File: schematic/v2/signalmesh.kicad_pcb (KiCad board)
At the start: 4 copper layers, 387 x 151 mm, 155 parts, among them J1 FPGA I/O, J10 INA219_CONFIG, J11 INA219_CONFIG, J12 AAM_DBG, J13 UUM_DBG, J14 ACM_DBG, J15 INA219_CONFIG, J16 DSM_DBG, J17 LCD_display, J18 LCD_display, J19 AudioJack3, J2 FPGA I/O, J3 LCD_display, J4 TDM_DBG, J5 INA219_CONFIG, J6 INA219_CONFIG, J7 INA219_CONFIG, J8 FPGA I/O, J9 FPGA I/O, U1 NUCLEO-H753ZI, U10 INA219AxD, U11 INA219AxD, U12 INA219AxD, U13 INA219AxD, U14 W25Q128JVS, U15 AP2112K-3.3, U16 74HC4050D, U17 NUCLEO-H753ZI, U18 HDSP-7503, U19 HDSP-7503, U2 HDSP-7503, U20 INA219AxD, U21 74HC4050D, U22 AP2112K-3.3, U23 W25Q128JVS, U24 74HC4050D, U25 AP2112K-3.3, U26 W25Q128JVS, U27 MCP2551-I-P, U28 74LVC1G3157, U29 MCP2551-I-P, U3 NUCLEO-F303RE, U30 MCP2551-I-P, U31 MCP2551-I-P, U4 YAAJ_BluePill_Part_Like, U5 24LC256-I_SN, U6 BME280, U7 INA219AxD, U8 24LC256-I_SN, U9 NUCLEO-F446RE

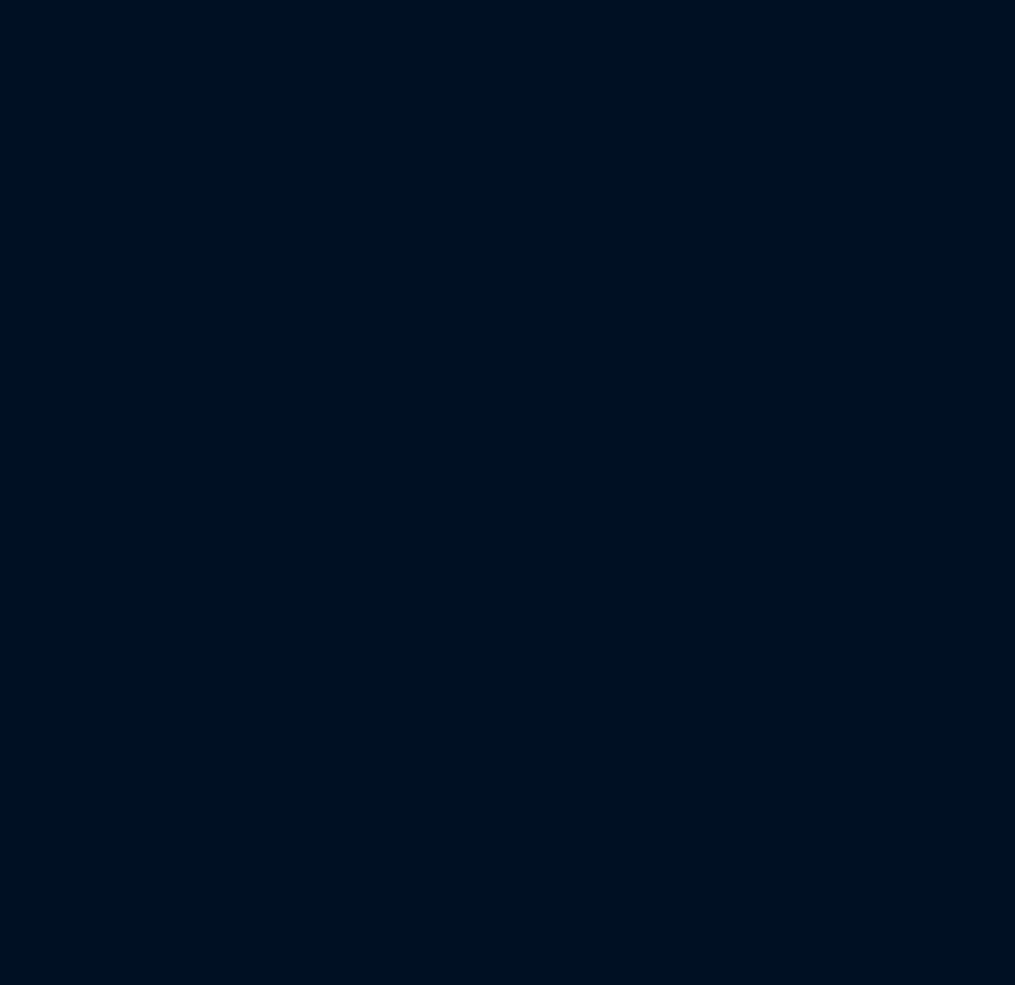
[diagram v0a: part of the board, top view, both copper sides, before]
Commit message: removing the courtyard from the filler plots. theyre not actually components just an outline with throughholes
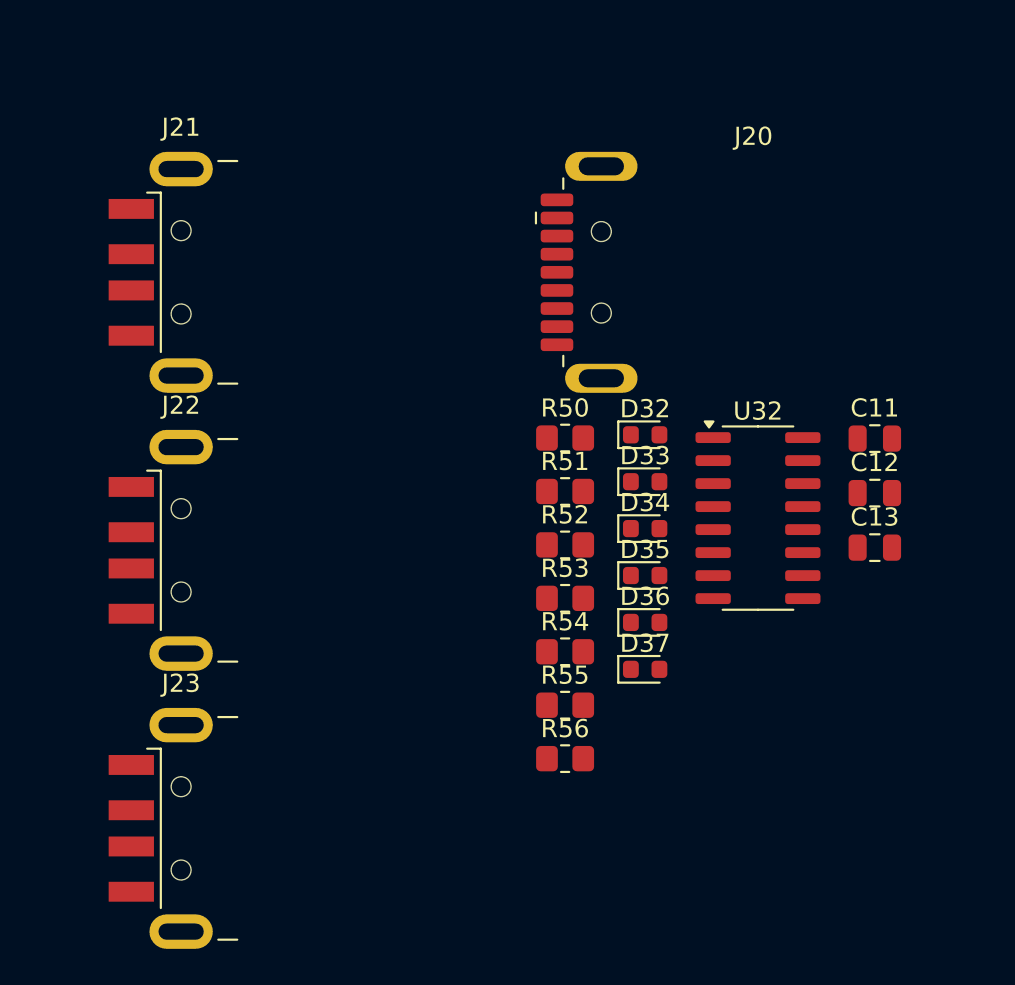
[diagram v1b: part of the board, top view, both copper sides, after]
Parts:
- added C11: 22pf, Capacitor_SMD:C_0805_2012Metric, F.Cu at (338.4, 232.9)
- added C12: 22pf, Capacitor_SMD:C_0805_2012Metric, F.Cu at (338.4, 235.9)
- added C13: 22pf, Capacitor_SMD:C_0805_2012Metric, F.Cu at (338.4, 238.9)
- added D32: LED_PWR, LED_SMD:LED_0603_1608Metric, F.Cu at (325.7, 232.7)
- added D33: LED_PWR, LED_SMD:LED_0603_1608Metric, F.Cu at (325.7, 235.3)
- added D34: LED_PWR, LED_SMD:LED_0603_1608Metric, F.Cu at (325.7, 237.9)
- added D35: TXD, LED_SMD:LED_0603_1608Metric, F.Cu at (325.7, 240.5)
- added D36: RXD, LED_SMD:LED_0603_1608Metric, F.Cu at (325.7, 243.1)
- added D37: LED_PWR, LED_SMD:LED_0603_1608Metric, F.Cu at (325.7, 245.7)
- added J20: USB3_A, Connector_USB:USB3_A_Plug_Wuerth_692112030100_Horizontal, F.Cu at (331.7, 223.8)
- added J21: USB_A, Connector_USB:USB_A_CNCTech_1001-011-01101_Horizontal, F.Cu at (307.0, 223.8)
- added J22: USB_A, Connector_USB:USB_A_CNCTech_1001-011-01101_Horizontal, F.Cu at (307.0, 239.1)
- added J23: USB_A, Connector_USB:USB_A_CNCTech_1001-011-01101_Horizontal, F.Cu at (307.0, 254.4)
- added R50: 300, Resistor_SMD:R_0805_2012Metric_Pad1.20x1.40mm_HandSolder, F.Cu at (321.3, 232.9)
- added R51: 300, Resistor_SMD:R_0805_2012Metric_Pad1.20x1.40mm_HandSolder, F.Cu at (321.3, 235.8)
- added R52: 300, Resistor_SMD:R_0805_2012Metric_Pad1.20x1.40mm_HandSolder, F.Cu at (321.3, 238.8)
- added R53: 300, Resistor_SMD:R_0805_2012Metric_Pad1.20x1.40mm_HandSolder, F.Cu at (321.3, 241.8)
- added R54: 300, Resistor_SMD:R_0805_2012Metric_Pad1.20x1.40mm_HandSolder, F.Cu at (321.3, 244.7)
- added R55: 1k5, Resistor_SMD:R_0805_2012Metric_Pad1.20x1.40mm_HandSolder, F.Cu at (321.3, 247.7)
- added R56: 300, Resistor_SMD:R_0805_2012Metric_Pad1.20x1.40mm_HandSolder, F.Cu at (321.3, 250.6)
- added U32: CH340G, Package_SO:SOIC-16_3.9x9.9mm_P1.27mm, F.Cu at (331.9, 237.3)
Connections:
- U1 pad CN12_12: unconnected-(U1B-PA12-PadCN12_12) -> AAM_USB_D-
- U1 pad CN12_14: unconnected-(U1B-PA11-PadCN12_14) -> AAM_USB_D+

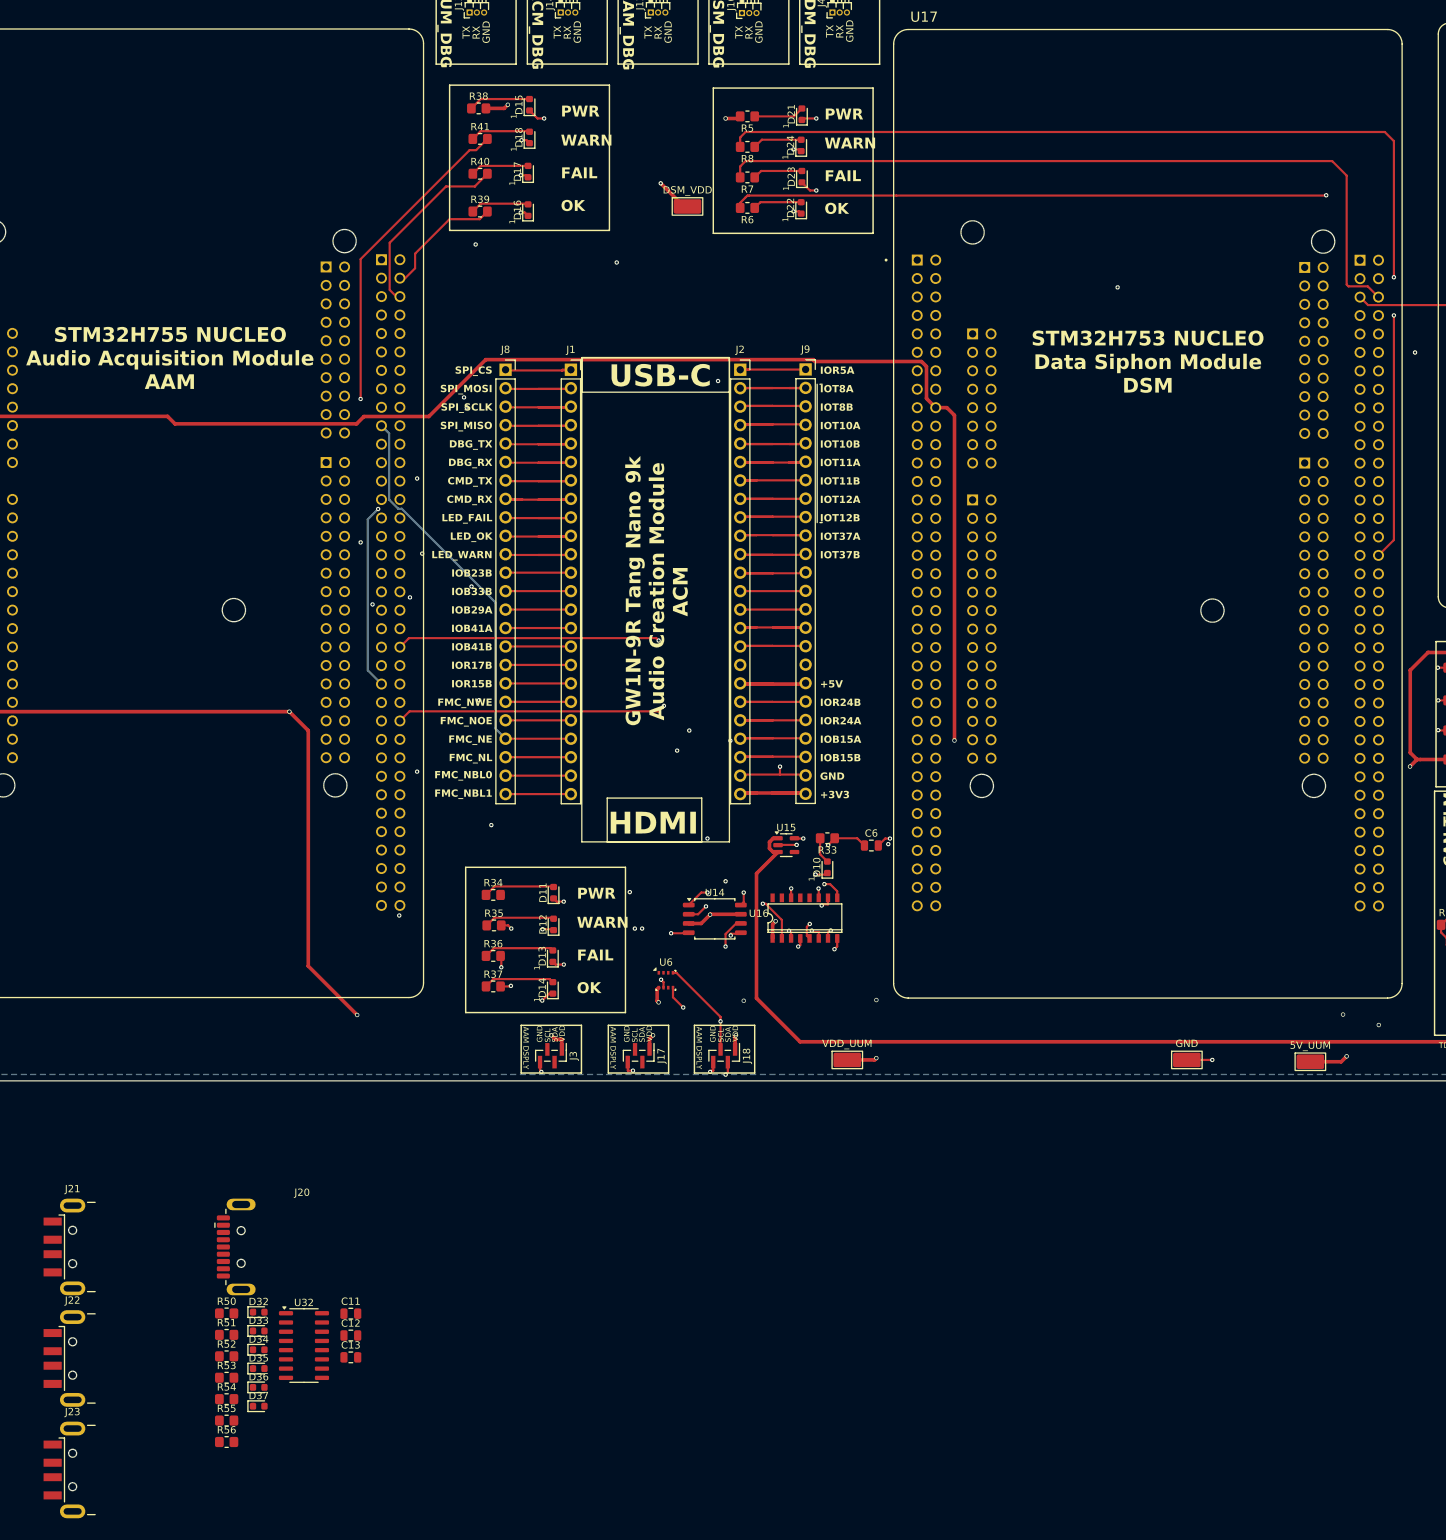
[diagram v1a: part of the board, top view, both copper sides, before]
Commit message: moving to multiple sheets for the schematic
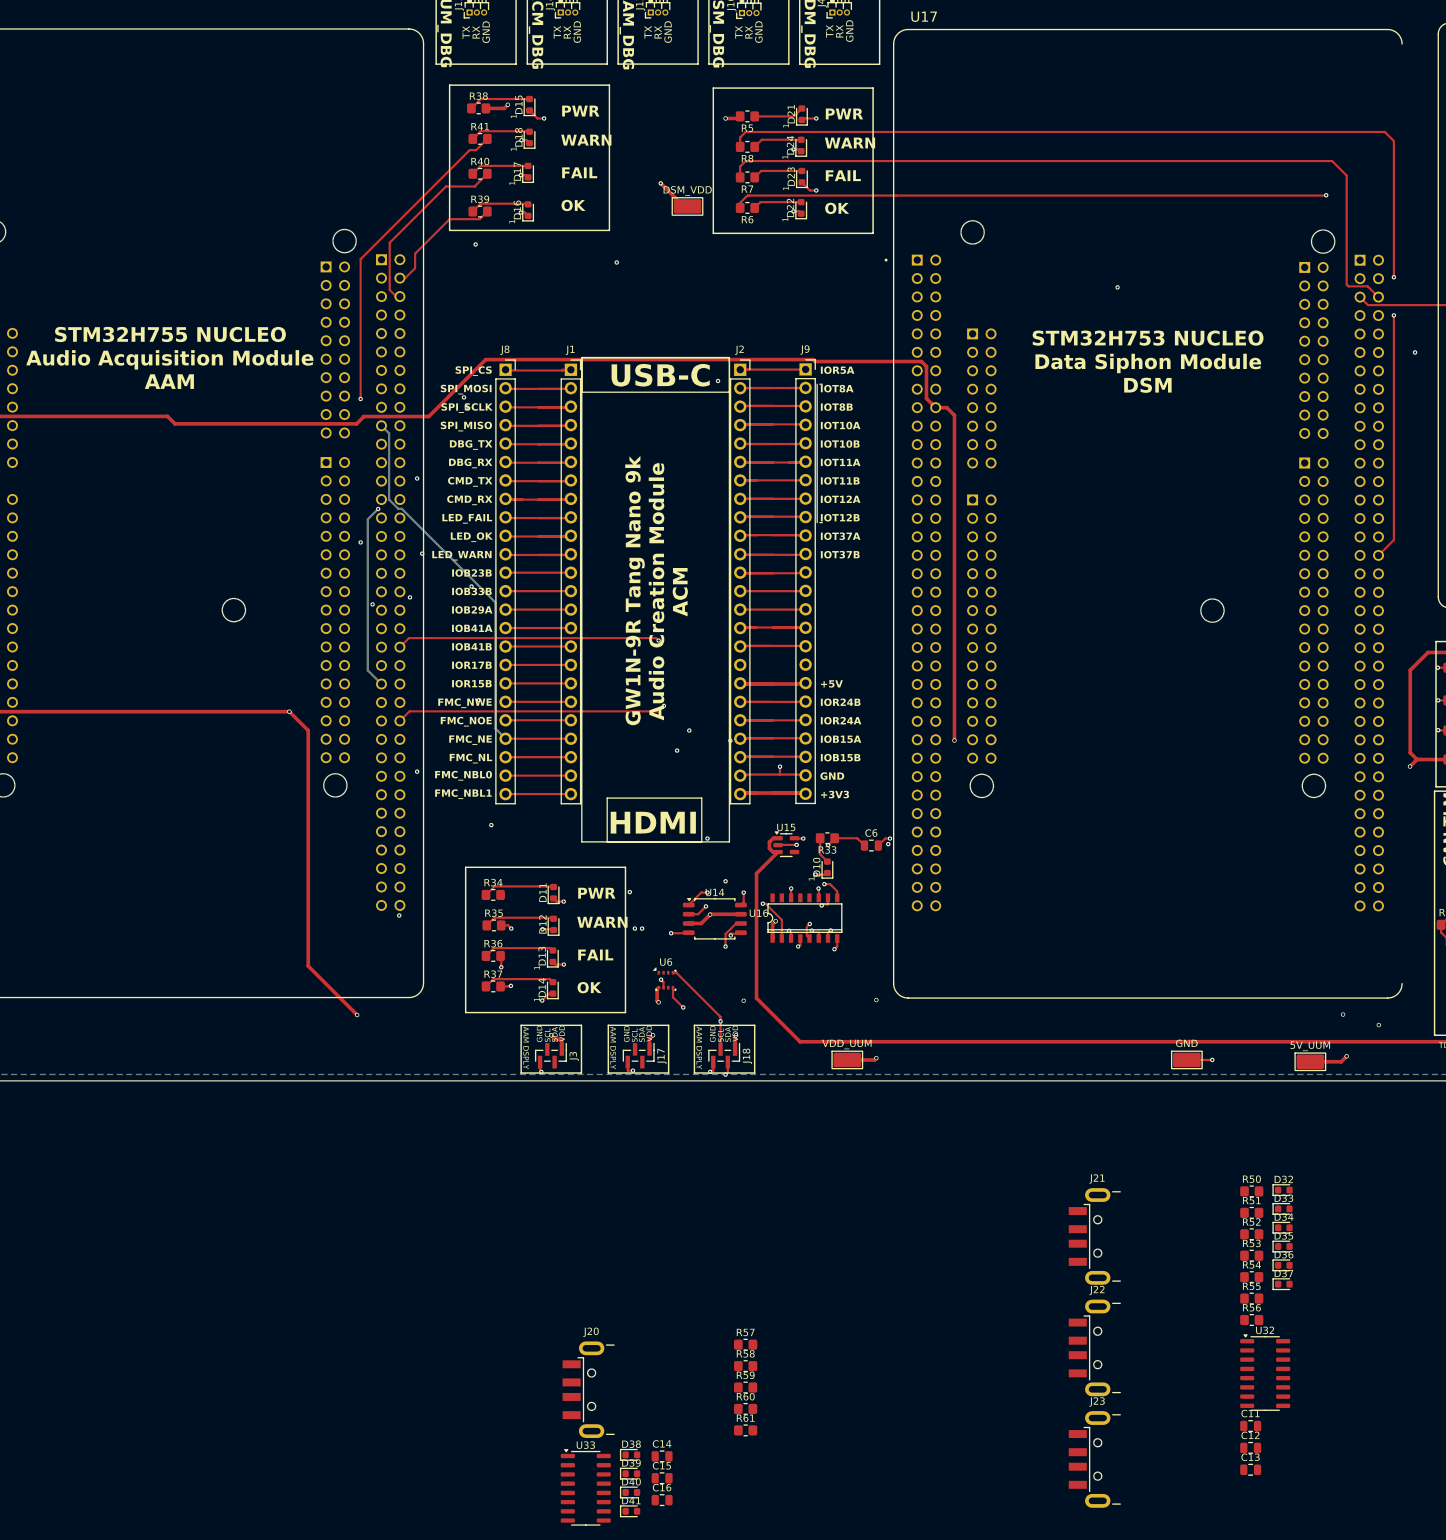
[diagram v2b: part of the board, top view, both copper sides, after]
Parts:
- added C14: 22pf, Capacitor_SMD:C_0805_2012Metric, F.Cu at (381.2, 252.6)
- added C15: 22pf, Capacitor_SMD:C_0805_2012Metric, F.Cu at (381.2, 255.6)
- added C16: 22pf, Capacitor_SMD:C_0805_2012Metric, F.Cu at (381.2, 258.6)
- added D38: LED_PWR, LED_SMD:LED_0603_1608Metric, F.Cu at (377.0, 252.4)
- added D39: LED_PWR, LED_SMD:LED_0603_1608Metric, F.Cu at (377.0, 255.0)
- added D40: TXD, LED_SMD:LED_0603_1608Metric, F.Cu at (377.0, 257.6)
- added D41: RXD, LED_SMD:LED_0603_1608Metric, F.Cu at (377.0, 260.1)
- added R57: 300, Resistor_SMD:R_0805_2012Metric_Pad1.20x1.40mm_HandSolder, F.Cu at (392.8, 237.2)
- added R58: 300, Resistor_SMD:R_0805_2012Metric_Pad1.20x1.40mm_HandSolder, F.Cu at (392.8, 240.2)
- added R59: 300, Resistor_SMD:R_0805_2012Metric_Pad1.20x1.40mm_HandSolder, F.Cu at (392.8, 243.1)
- added R60: 300, Resistor_SMD:R_0805_2012Metric_Pad1.20x1.40mm_HandSolder, F.Cu at (392.8, 246.1)
- added R61: 1k5, Resistor_SMD:R_0805_2012Metric_Pad1.20x1.40mm_HandSolder, F.Cu at (392.8, 249.0)
- added U33: CH340G, Package_SO:SOIC-16_3.9x9.9mm_P1.27mm, F.Cu at (370.8, 257.0)
- J20: value USB3_A -> USB_A; footprint Connector_USB:USB3_A_Plug_Wuerth_692112030100_Horizontal -> Connector_USB:USB_A_CNCTech_1001-011-01101_Horizontal
- moved D32 142.1 mm to (466.9, 215.9)
- moved D33 142.1 mm to (466.9, 218.5)
- moved D34 142.1 mm to (466.9, 221.1)
- moved D35 142.1 mm to (466.9, 223.7)
- moved D36 142.1 mm to (466.9, 226.3)
- moved R50 142.1 mm to (462.4, 216.1)
- moved R52 142.1 mm to (462.4, 222.0)
- moved R53 142.1 mm to (462.4, 224.9)
- moved R55 142.1 mm to (462.4, 230.8)
- moved D37 142.1 mm to (466.9, 228.9)
- moved R51 142.1 mm to (462.4, 219.1)
- moved R54 142.1 mm to (462.4, 227.9)
- moved R56 142.1 mm to (462.4, 233.8)
- moved J21 141.1 mm to (448.1, 222.3)
- moved J22 141.1 mm to (448.1, 237.7)
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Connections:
- J20 pad 1: unconnected-(J20-VBUS-Pad1) -> DSM_VDD
- J20 pad 2: unconnected-(J20-D--Pad2) -> Net-(J20-D-)
- J20 pad 3: unconnected-(J20-D+-Pad3) -> Net-(J20-D+)
- J20 pad 4: unconnected-(J20-GND-Pad4) -> GND
- J22 pad 1: AAM_VDD -> DSM_VDD
- J22 pad 2: AAM_USB_D- -> DSM_USB_D-
- J22 pad 3: AAM_USB_D+ -> DSM_USB_D+
- R56 pad 2: AAM_VDD -> DSM_VDD

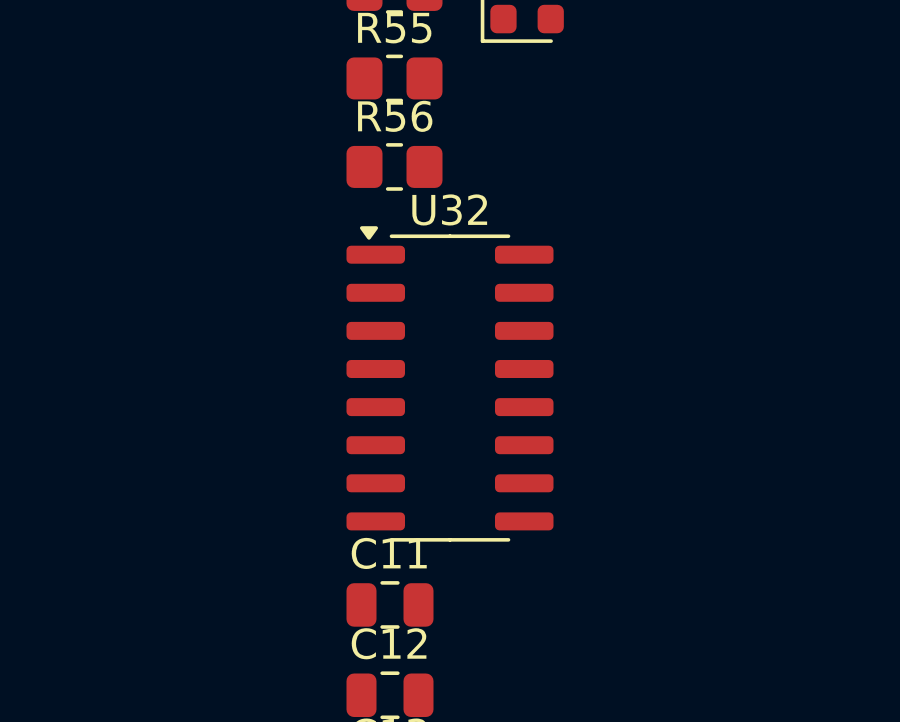
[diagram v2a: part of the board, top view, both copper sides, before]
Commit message: v2 updates. remove sniffer
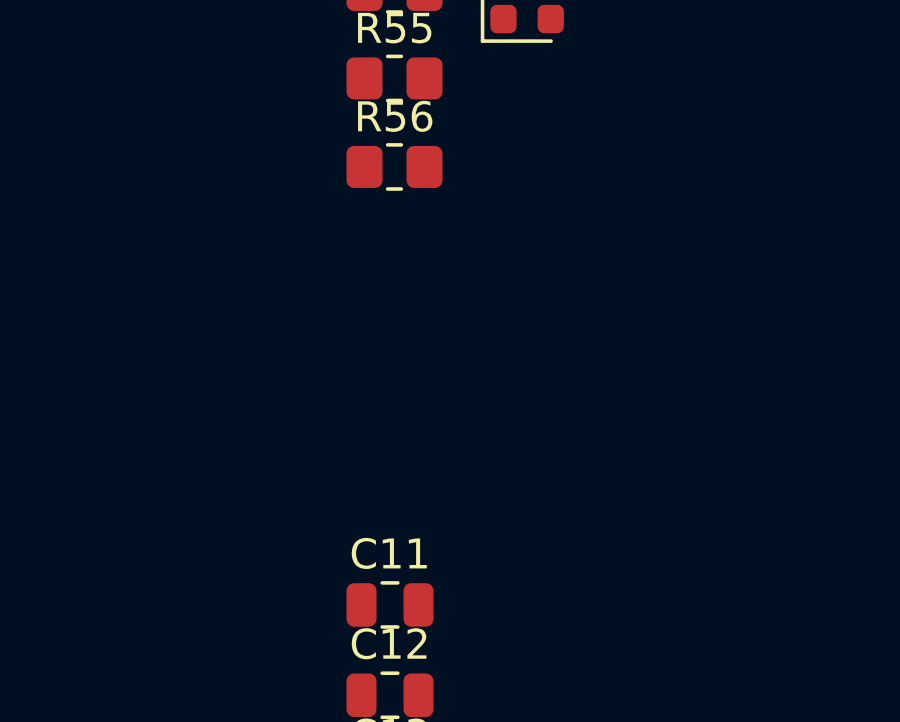
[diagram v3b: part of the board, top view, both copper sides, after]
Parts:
- removed U32: CH340G, Package_SO:SOIC-16_3.9x9.9mm_P1.27mm
